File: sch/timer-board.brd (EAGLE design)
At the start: 76.2 x 69.9 mm, 33 parts, among them IC1 ATMEGA328P

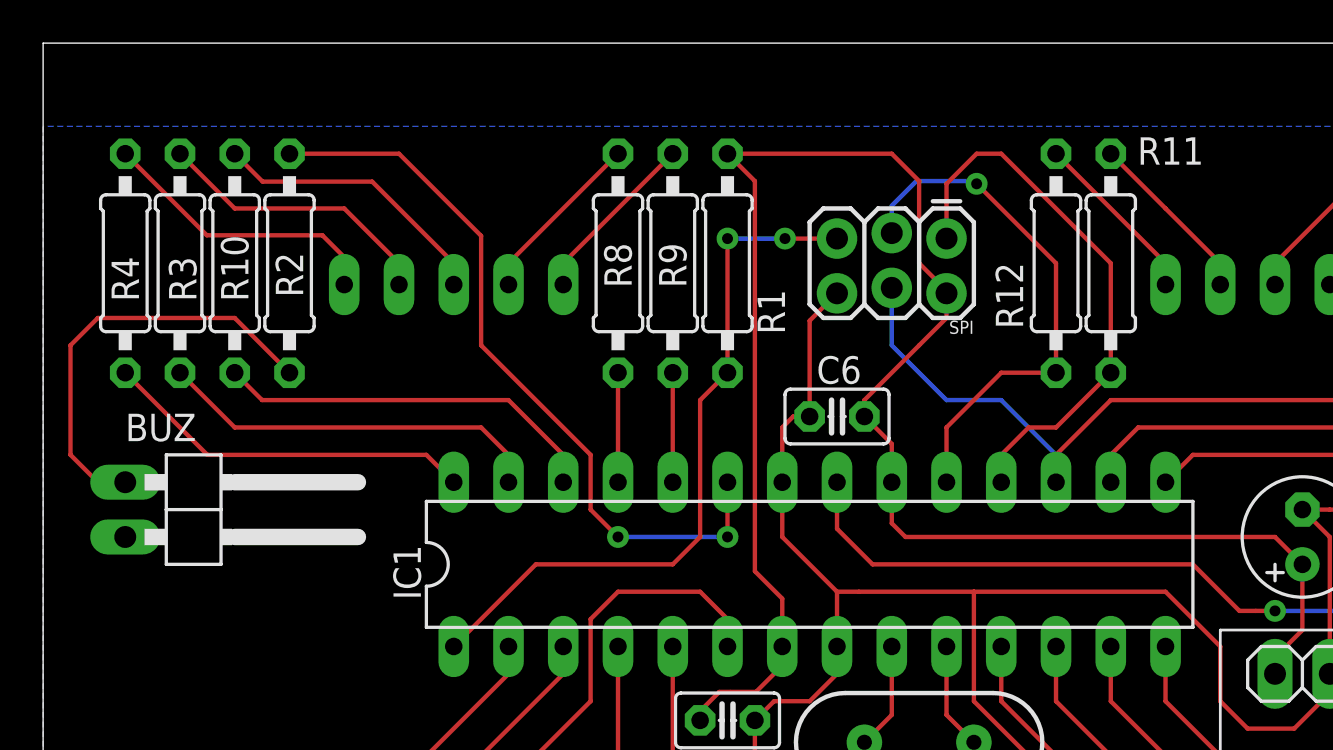
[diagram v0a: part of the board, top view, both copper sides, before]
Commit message: PCB : better label positioning
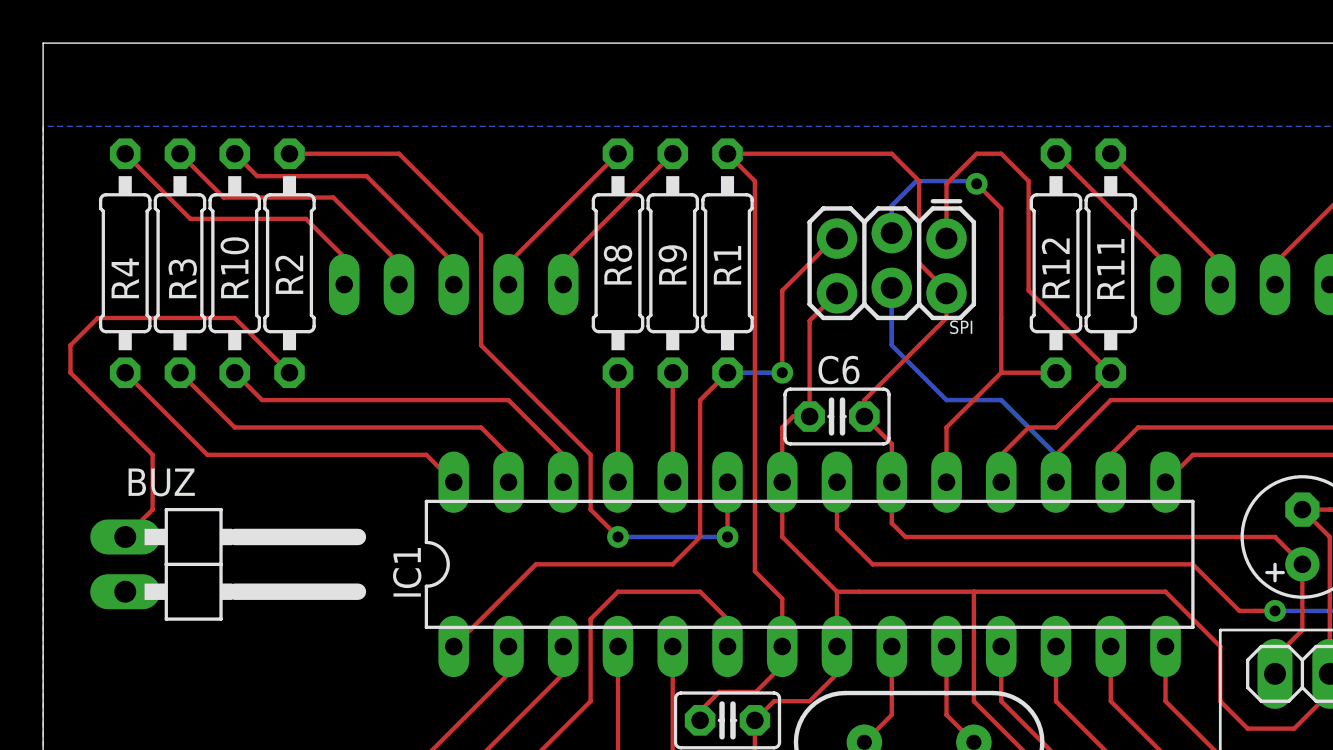
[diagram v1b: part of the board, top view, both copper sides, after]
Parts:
- moved BUZ 2.54 mm to (7.62, 45.7)
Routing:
- net N$8: track 19.9 -> 22.7 mm
- net RST: track 33.0 -> 31.6 mm, vias 2 -> 1
- net D0B: track 24.7 -> 23.6 mm
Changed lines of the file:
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@@
 </element>
 <element name="R11" library="rcl" library_urn="urn:adsk.eagle:library:334" package="0207/10" package3d_urn="urn:adsk.eagle:package:23491/1" value="" x="49.53" y="59.69" smashed="yes" rot="R90">
-<attribute name="NAME" x="53.848" y="65.532" size="1.27" layer="25" ratio="10" rot="R180"/>
+<attribute name="NAME" x="48.895" y="60.96" size="1.27" layer="25" ratio="10" rot="R270"/>
 <attribute name="SPICEPREFIX" value="R" x="49.53" y="59.69" size="1.778" layer="27" rot="R90" display="off"/>
 <attribute name="VALUE" x="50.165" y="57.4294" size="1.27" layer="27" ratio="10" rot="R90"/>
 </element>
 <element name="R12" library="rcl" library_urn="urn:adsk.eagle:library:334" package="0207/10" package3d_urn="urn:adsk.eagle:package:23491/1" value="" x="46.99" y="59.69" smashed="yes" rot="R90">
-<attribute name="NAME" x="45.466" y="56.642" size="1.27" layer="25" ratio="10" rot="R90"/>
+<attribute name="NAME" x="47.625" y="57.912" size="1.27" layer="25" ratio="10" rot="R90"/>
 <attribute name="SPICEPREFIX" value="R" x="46.99" y="59.69" size="1.778" layer="27" rot="R90" display="off"/>
 <attribute name="VALUE" x="47.625" y="57.4294" size="1.27" layer="27" ratio="10" rot="R90"/>
@@
 </element>
 <element name="R1" library="rcl" library_urn="urn:adsk.eagle:library:334" package="0207/10" package3d_urn="urn:adsk.eagle:package:23491/1" value="10k" x="31.75" y="59.69" smashed="yes" rot="R90">
-<attribute name="NAME" x="34.417" y="56.388" size="1.27" layer="25" ratio="10" rot="R90"/>
+<attribute name="NAME" x="32.385" y="58.547" size="1.27" layer="25" ratio="10" rot="R90"/>
 <attribute name="SPICEPREFIX" value="R" x="31.75" y="59.69" size="1.778" layer="27" rot="R90" display="off"/>
 </element>
@@
 <attribute name="SPICEPREFIX" value="C" x="36.83" y="52.578" size="1.778" layer="27" rot="R180" display="off"/>
 </element>
-<element name="BUZ" library="pinhead" library_urn="urn:adsk.eagle:library:325" package="1X02/90" package3d_urn="urn:adsk.eagle:package:22437/2" value="" x="7.62" y="48.26" rot="R270"/>
+<element name="BUZ" library="pinhead" library_urn="urn:adsk.eagle:library:325" package="1X02/90" package3d_urn="urn:adsk.eagle:package:22437/2" value="" x="7.62" y="45.72" rot="R270"/>
 <element name="ENC" library="parts" package="1X5_ANGLE" value="" x="55.88" y="21.59" smashed="yes" rot="R90">
 <attribute name="NAME" x="54.864" y="15.748" size="1.27" layer="25" ratio="10" rot="R180"/>
@@
 <wire x1="30.48" y1="46.99" x2="30.48" y2="53.34" width="0.2032" layer="1"/>
 <wire x1="30.48" y1="53.34" x2="31.75" y2="54.61" width="0.2032" layer="1"/>
-<wire x1="36.83" y1="60.833" x2="34.417" y2="60.833" width="0.2032" layer="1"/>
-<via x="34.417" y="60.833" extent="1-16" drill="0.508"/>
-<wire x1="34.417" y1="60.833" x2="31.75" y2="60.833" width="0.2032" layer="16"/>
-<via x="31.75" y="60.833" extent="1-16" drill="0.508"/>
-<wire x1="31.75" y1="60.833" x2="31.75" y2="54.61" width="0.2032" layer="1"/>
+<via x="34.29" y="54.61" extent="1-16" drill="0.508"/>
+<wire x1="34.29" y1="58.42" x2="36.703" y2="60.833" width="0.2032" layer="1"/>
+<wire x1="36.703" y1="60.833" x2="36.83" y2="60.833" width="0.2032" layer="1"/>
+<wire x1="34.29" y1="54.61" x2="34.29" y2="58.42" width="0.2032" layer="1"/>
+<wire x1="31.75" y1="54.61" x2="34.29" y2="54.61" width="0.2032" layer="16"/>
 </signal>
 <signal name="ENC2">
@@
 <contactref element="R3" pad="2"/>
 <contactref element="DIGIT1" pad="9"/>
-<wire x1="6.35" y1="64.77" x2="8.89" y2="62.23" width="0.2032" layer="1"/>
-<wire x1="8.89" y1="62.23" x2="13.97" y2="62.23" width="0.2032" layer="1"/>
-<wire x1="13.97" y1="62.23" x2="16.51" y2="59.69" width="0.2032" layer="1"/>
+<wire x1="6.35" y1="64.77" x2="8.382" y2="62.738" width="0.2032" layer="1"/>
+<wire x1="8.382" y1="62.738" x2="13.462" y2="62.738" width="0.2032" layer="1"/>
+<wire x1="13.462" y1="62.738" x2="16.51" y2="59.69" width="0.2032" layer="1"/>
 <wire x1="16.51" y1="59.69" x2="16.51" y2="58.6994" width="0.2032" layer="1"/>
 </signal>
@@
 <contactref element="DIGIT1" pad="10"/>
 <contactref element="R4" pad="2"/>
-<wire x1="12.954" y1="60.9854" x2="7.5946" y2="60.9854" width="0.2032" layer="1"/>
-<wire x1="7.5946" y1="60.9854" x2="3.81" y2="64.77" width="0.2032" layer="1"/>
-<wire x1="13.97" y1="59.9694" x2="12.954" y2="60.9854" width="0.2032" layer="1"/>
+<wire x1="12.192" y1="61.7474" x2="6.8326" y2="61.7474" width="0.2032" layer="1"/>
+<wire x1="6.8326" y1="61.7474" x2="3.81" y2="64.77" width="0.2032" layer="1"/>
+<wire x1="13.97" y1="59.9694" x2="12.192" y2="61.7474" width="0.2032" layer="1"/>
 <wire x1="13.97" y1="58.6994" x2="13.97" y2="59.9694" width="0.2032" layer="1"/>
 </signal>
@@
 <contactref element="R10" pad="2"/>
 <wire x1="19.05" y1="58.6994" x2="19.05" y2="59.69" width="0.2032" layer="1"/>
-<wire x1="19.05" y1="59.69" x2="15.2654" y2="63.4746" width="0.2032" layer="1"/>
-<wire x1="10.1854" y1="63.4746" x2="8.89" y2="64.77" width="0.2032" layer="1"/>
-<wire x1="15.2654" y1="63.4746" x2="10.1854" y2="63.4746" width="0.2032" layer="1"/>
+<wire x1="19.05" y1="59.69" x2="15.0114" y2="63.7286" width="0.2032" layer="1"/>
+<wire x1="9.9314" y1="63.7286" x2="8.89" y2="64.77" width="0.2032" layer="1"/>
+<wire x1="15.0114" y1="63.7286" x2="9.9314" y2="63.7286" width="0.2032" layer="1"/>
 </signal>
 <signal name="N$13">
@@
 <wire x1="41.91" y1="63.373" x2="43.307" y2="64.77" width="0.2032" layer="1"/>
 <wire x1="43.307" y1="64.77" x2="44.45" y2="64.77" width="0.2032" layer="1"/>
-<wire x1="44.45" y1="64.77" x2="49.53" y2="59.69" width="0.2032" layer="1"/>
-<wire x1="49.53" y1="59.69" x2="49.53" y2="54.61" width="0.2032" layer="1"/>
+<wire x1="44.45" y1="64.77" x2="45.72" y2="63.5" width="0.2032" layer="1"/>
+<wire x1="45.72" y1="63.5" x2="45.72" y2="58.42" width="0.2032" layer="1"/>
 <wire x1="41.91" y1="60.833" x2="41.91" y2="63.373" width="0.2032" layer="1"/>
 <wire x1="46.99" y1="52.07" x2="45.72" y2="52.07" width="0.2032" layer="1"/>
 <wire x1="45.72" y1="52.07" x2="44.45" y2="50.8" width="0.2032" layer="1"/>
 <wire x1="44.45" y1="50.8" x2="44.45" y2="49.53" width="0.2032" layer="1"/>
+<wire x1="45.72" y1="58.42" x2="49.53" y2="54.61" width="0.2032" layer="1"/>
 </signal>
 <signal name="D0B">
@@
 <wire x1="40.513" y1="63.5" x2="43.18" y2="63.5" width="0.2032" layer="16"/>
 <via x="43.307" y="63.373" extent="1-16" drill="0.508"/>
-<wire x1="43.307" y1="63.373" x2="46.99" y2="59.69" width="0.2032" layer="1"/>
-<wire x1="46.99" y1="59.69" x2="46.99" y2="54.61" width="0.2032" layer="1"/>
+<wire x1="43.307" y1="63.373" x2="44.45" y2="62.23" width="0.2032" layer="1"/>
+<wire x1="44.45" y1="62.23" x2="44.45" y2="57.15" width="0.2032" layer="1"/>
 <wire x1="43.18" y1="63.5" x2="43.307" y2="63.373" width="0.2032" layer="16"/>
 <wire x1="39.37" y1="61.087" x2="39.37" y2="62.357" width="0.2032" layer="16"/>
+<wire x1="44.45" y1="57.15" x2="44.45" y2="54.61" width="0.2032" layer="1"/>
 </signal>
 <signal name="D0C">
@@
 <contactref element="R2" pad="2"/>
 <contactref element="BUZ" pad="1"/>
-<wire x1="2.54" y1="49.53" x2="1.27" y2="50.8" width="0.2032" layer="1"/>
-<wire x1="1.27" y1="50.8" x2="1.27" y2="55.88" width="0.2032" layer="1"/>
-<wire x1="1.27" y1="55.88" x2="2.54" y2="57.15" width="0.2032" layer="1"/>
-<wire x1="2.54" y1="57.15" x2="8.89" y2="57.15" width="0.2032" layer="1"/>
-<wire x1="8.89" y1="57.15" x2="11.43" y2="54.61" width="0.2032" layer="1"/>
-<wire x1="3.81" y1="49.53" x2="2.54" y2="49.53" width="0.2032" layer="1"/>
+<wire x1="11.43" y1="54.61" x2="8.89" y2="57.15" width="0.2032" layer="1"/>
+<wire x1="5.08" y1="50.8" x2="5.08" y2="48.26" width="0.2032" layer="1"/>
+<wire x1="2.54" y1="57.15" x2="1.27" y2="55.88" width="0.2032" layer="1"/>
+<wire x1="1.27" y1="55.88" x2="1.27" y2="54.61" width="0.2032" layer="1"/>
+<wire x1="1.27" y1="54.61" x2="5.08" y2="50.8" width="0.2032" layer="1"/>
+<wire x1="8.89" y1="57.15" x2="2.54" y2="57.15" width="0.2032" layer="1"/>
+<wire x1="5.08" y1="48.26" x2="3.81" y2="46.99" width="0.2032" layer="1"/>
 </signal>
 <signal name="VIN">

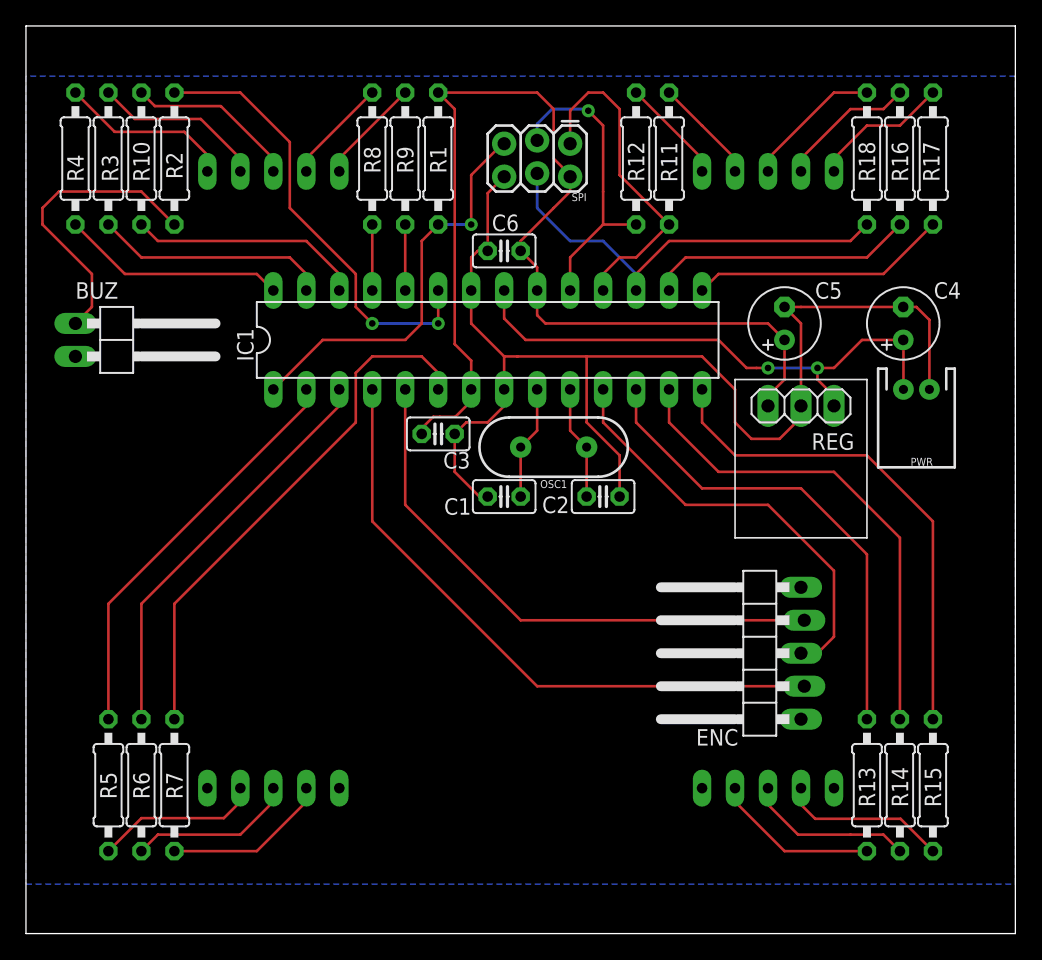
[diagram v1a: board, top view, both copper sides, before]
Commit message: PCB : Added some logos
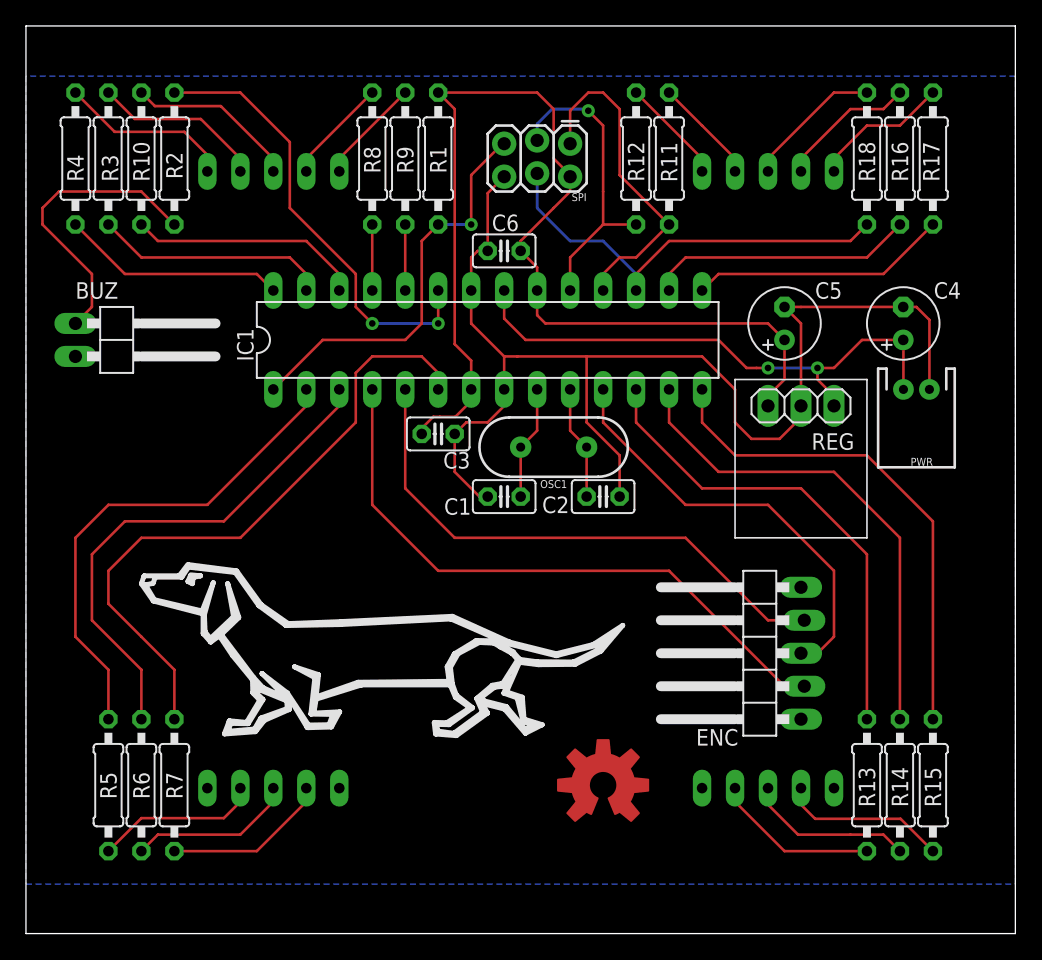
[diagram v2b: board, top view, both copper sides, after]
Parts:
- added LOGO1: OSHW-LOGOL-COPPER, SparkFun-Aesthetics:OSHW-LOGO-L_COPPER
- added U$1: DOG_LOGO, parts:DOG
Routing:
- net D1E: track 41.1 -> 49.8 mm
- net D1D: track 31.7 -> 39.3 mm
- net D1C: track 31.7 -> 38.3 mm
- net ENC2: track 48.7 -> 48.0 mm
- net ENC1: track 43.3 -> 42.6 mm
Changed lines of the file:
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@@
 <attribute name="VALUE" x="55.88" y="34.925" size="1.27" layer="27"/>
 </element>
+<element name="LOGO1" library="SparkFun-Aesthetics" library_urn="urn:adsk.eagle:library:507" package="OSHW-LOGO-L_COPPER" package3d_urn="urn:adsk.eagle:package:37117/1" value="OSHW-LOGOL-COPPER" x="44.45" y="11.43"/>
+<element name="U$1" library="parts" package="DOG" value="DOG_LOGO" x="8.89" y="15.24"/>
 </elements>
 <signals>
@@
 <signal name="ENC2">
 <contactref element="IC1" pad="4"/>
-<wire x1="26.67" y1="31.75" x2="26.67" y2="41.91" width="0.2032" layer="1"/>
 <contactref element="ENC" pad="2"/>
-<wire x1="39.37" y1="19.05" x2="26.67" y2="31.75" width="0.2032" layer="1"/>
-<wire x1="59.944" y1="19.05" x2="39.37" y2="19.05" width="0.2032" layer="1"/>
+<wire x1="26.67" y1="33.02" x2="31.75" y2="27.94" width="0.2032" layer="1"/>
+<wire x1="31.75" y1="27.94" x2="49.53" y2="27.94" width="0.2032" layer="1"/>
+<wire x1="49.53" y1="27.94" x2="58.42" y2="19.05" width="0.2032" layer="1"/>
+<wire x1="58.42" y1="19.05" x2="59.944" y2="19.05" width="0.2032" layer="1"/>
+<wire x1="26.67" y1="41.91" x2="26.67" y2="33.02" width="0.2032" layer="1"/>
 </signal>
 <signal name="ENC1">
 <contactref element="IC1" pad="5"/>
-<wire x1="29.21" y1="41.91" x2="29.21" y2="33.02" width="0.2032" layer="1"/>
 <contactref element="ENC" pad="4"/>
-<wire x1="59.944" y1="24.13" x2="38.1" y2="24.13" width="0.2032" layer="1"/>
-<wire x1="38.1" y1="24.13" x2="29.21" y2="33.02" width="0.2032" layer="1"/>
+<wire x1="29.21" y1="41.91" x2="29.21" y2="34.29" width="0.2032" layer="1"/>
+<wire x1="29.21" y1="34.29" x2="33.02" y2="30.48" width="0.2032" layer="1"/>
+<wire x1="50.8" y1="30.48" x2="57.15" y2="24.13" width="0.2032" layer="1"/>
+<wire x1="57.15" y1="24.13" x2="59.944" y2="24.13" width="0.2032" layer="1"/>
+<wire x1="33.02" y1="30.48" x2="50.8" y2="30.48" width="0.2032" layer="1"/>
 </signal>
 <signal name="BTN">
@@
 <contactref element="R5" pad="1"/>
 <contactref element="IC1" pad="2"/>
-<wire x1="21.59" y1="41.91" x2="21.59" y2="40.64" width="0.2032" layer="1"/>
-<wire x1="21.59" y1="40.64" x2="6.35" y2="25.4" width="0.2032" layer="1"/>
-<wire x1="6.35" y1="25.4" x2="6.35" y2="16.51" width="0.2032" layer="1"/>
+<wire x1="21.59" y1="40.64" x2="21.59" y2="41.91" width="0.2032" layer="1"/>
+<wire x1="6.35" y1="16.51" x2="6.35" y2="20.32" width="0.2032" layer="1"/>
+<wire x1="6.35" y1="20.32" x2="3.81" y2="22.86" width="0.2032" layer="1"/>
+<wire x1="6.35" y1="33.02" x2="13.97" y2="33.02" width="0.2032" layer="1"/>
+<wire x1="13.97" y1="33.02" x2="21.59" y2="40.64" width="0.2032" layer="1"/>
+<wire x1="3.81" y1="22.86" x2="3.81" y2="30.48" width="0.2032" layer="1"/>
+<wire x1="3.81" y1="30.48" x2="6.35" y2="33.02" width="0.2032" layer="1"/>
 </signal>
 <signal name="D1D">
@@
 <contactref element="IC1" pad="3"/>
 <wire x1="24.13" y1="41.91" x2="24.13" y2="40.64" width="0.2032" layer="1"/>
-<wire x1="24.13" y1="40.64" x2="8.89" y2="25.4" width="0.2032" layer="1"/>
-<wire x1="8.89" y1="25.4" x2="8.89" y2="16.51" width="0.2032" layer="1"/>
+<wire x1="15.24" y1="31.75" x2="7.62" y2="31.75" width="0.2032" layer="1"/>
+<wire x1="7.62" y1="31.75" x2="5.08" y2="29.21" width="0.2032" layer="1"/>
+<wire x1="5.08" y1="29.21" x2="5.08" y2="24.13" width="0.2032" layer="1"/>
+<wire x1="5.08" y1="24.13" x2="8.89" y2="20.32" width="0.2032" layer="1"/>
+<wire x1="8.89" y1="20.32" x2="8.89" y2="16.51" width="0.2032" layer="1"/>
+<wire x1="24.13" y1="40.64" x2="15.24" y2="31.75" width="0.2032" layer="1"/>
 </signal>
 <signal name="D1E">
 <contactref element="R7" pad="1"/>
 <contactref element="IC1" pad="6"/>
-<wire x1="11.43" y1="16.51" x2="11.43" y2="25.4" width="0.2032" layer="1"/>
-<wire x1="11.43" y1="25.4" x2="25.4" y2="39.37" width="0.2032" layer="1"/>
-<wire x1="25.4" y1="39.37" x2="25.4" y2="43.18" width="0.2032" layer="1"/>
-<wire x1="25.4" y1="43.18" x2="26.67" y2="44.45" width="0.2032" layer="1"/>
+<wire x1="26.67" y1="44.45" x2="25.4" y2="43.18" width="0.2032" layer="1"/>
 <wire x1="26.67" y1="44.45" x2="30.48" y2="44.45" width="0.2032" layer="1"/>
 <wire x1="30.48" y1="44.45" x2="31.75" y2="43.18" width="0.2032" layer="1"/>
 <wire x1="31.75" y1="43.18" x2="31.75" y2="41.91" width="0.2032" layer="1"/>
+<wire x1="25.4" y1="43.18" x2="25.4" y2="39.37" width="0.2032" layer="1"/>
+<wire x1="25.4" y1="39.37" x2="16.51" y2="30.48" width="0.2032" layer="1"/>
+<wire x1="8.89" y1="30.48" x2="6.35" y2="27.94" width="0.2032" layer="1"/>
+<wire x1="6.35" y1="27.94" x2="6.35" y2="25.4" width="0.2032" layer="1"/>
+<wire x1="6.35" y1="25.4" x2="8.89" y2="22.86" width="0.2032" layer="1"/>
+<wire x1="16.51" y1="30.48" x2="8.89" y2="30.48" width="0.2032" layer="1"/>
+<wire x1="8.89" y1="22.86" x2="11.43" y2="20.32" width="0.2032" layer="1"/>
+<wire x1="11.43" y1="20.32" x2="11.43" y2="16.51" width="0.2032" layer="1"/>
 </signal>
 <signal name="D1F">
